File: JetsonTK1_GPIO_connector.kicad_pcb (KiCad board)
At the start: 2 copper layers, 50 x 80 mm, 79 parts, among them J1 Screw_Terminal_1x03, P1 CONN_01X25, P10 CONN_01X10, P11 CONN_01X02, P12 CONN_01X03, P2 CONN_02X25, P3 CONN_02X25, P4 CONN_01X01, P5 CONN_01X04, P6 CONN_01X04, P7 CONN_01X04, P8 CONN_01X04, P9 CONN_02X10, Q1 BSS138PS, Q2 BSS138PS, Q3 BSS138PS, U1 TXB0108PW, U2 PCAL9555APW, U3 TXB0108PW, U4 MCP25625-E/SS, Y1 Crystal_GND24

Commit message: 進捗
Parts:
- removed Q1, Q2, Q3: BSS138PS, SMD_Packages:SOT363
- removed the R10 at (158.7, 52.9)
- removed the R11 at (114.9, 99.5)
- removed the R13 at (160.2, 64.6)
- removed the R15 at (158.7, 58.7)
- removed the R17 at (136.1, 87.1)
- removed the R3 at (124.9, 93.2)
- removed the R4 at (139.4, 81.3)
- removed the R5 at (121.8, 93.2)
- removed the R6 at (118.1, 99.5)
- removed the R7 at (111.8, 99.5)
- removed the R8 at (161.8, 52.9)
- removed the R9 at (136.4, 81.3)
- added C15: C, Capacitors_SMD:C_0603, F.Cu at (68.4, 92.9)
- added C16: C, Capacitors_SMD:C_0603, F.Cu at (74.2, 91.5)
- added C6: C, Capacitors_SMD:C_0603, F.Cu at (73.8, 137.2)
- added C7: C, Capacitors_SMD:C_0603, F.Cu at (79.6, 135.8)
- added C8: C, Capacitors_SMD:C_0603, F.Cu at (73.8, 129.7)
- added C9: C, Capacitors_SMD:C_0603, F.Cu at (79.6, 128.3)
- added R14: R, Resistors_SMD:R_0603, F.Cu at (83.1, 135.1)
- added R19: R, Resistors_SMD:R_0603, F.Cu at (83.1, 127.6)
- added R25: R, Resistors_SMD:R_0603, F.Cu at (77.7, 90.8)
- added U4: PCA9306, Housings_SSOP:MSOP-8_3x3mm_Pitch0.65mm, F.Cu at (78.0, 138.5)
- added U5: PCA9306, Housings_SSOP:MSOP-8_3x3mm_Pitch0.65mm, F.Cu at (78.0, 131.0)
- added U7: PCA9306, Housings_SSOP:MSOP-8_3x3mm_Pitch0.65mm, F.Cu at (72.6, 94.2)
- JP1, JP2, JP3, JP4, JP5, JP6, JP7, JP8: moved to B.Cu
- P10: footprint Pin_Headers:Pin_Header_Straight_1x10 -> Connectors_JST:JST_XH_B10B-XH-A_10x2.50mm_Straight
- P5, P6, P7, P8: footprint Pin_Headers:Pin_Header_Straight_1x04 -> Connectors_JST:JST_XH_B04B-XH-A_04x2.50mm_Straight
- P9: footprint Pin_Headers:Pin_Header_Straight_2x10 -> Connect:IDC_Header_Straight_20pins
- moved P5 186.0 mm to (89.5, 137.0), turned to 0 degrees
- moved U3 174.0 mm to (67.0, 145.0), turned to 315 degrees
- moved P7 173.4 mm to (89.5, 114.5), turned to 0 degrees
- moved P8 173.2 mm to (89.5, 122.0), turned to 0 degrees
- moved P6 173.0 mm to (89.5, 129.5), turned to 0 degrees
- moved U1 168.0 mm to (68.8, 104.7)
- moved P1 165.8 mm to (51.5, 100.5)
- moved P2 165.8 mm to (53.5, 100.5)
- moved P3 165.8 mm to (57.5, 100.5)
- moved Y1 165.1 mm to (70.4, 112.5)
- moved P9 164.2 mm to (70.0, 77.0), turned to 0 degrees
- moved U6 163.6 mm to (82.6, 103.7)
- moved U2 162.6 mm to (80.7, 86.0), turned to 270 degrees
- moved J1 162.2 mm to (94.8, 107.8), turned to 90 degrees
- moved P10 156.0 mm to (97.0, 151.0), turned to 180 degrees
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- renumbered C6 to C10, C7 to C11, C8 to C12, C9 to C13, C10 to C14, R22 to R10, R23 to R11, R24 to R12, R25 to R13, R26 to R15, R27 to R16, R28 to R17, R29 to R18, R30 to R20, R31 to R21, R32 to R22, R33 to R23, R34 to R24, R35 to R26, R36 to R27, R12 to R3, R14 to R4, R16 to R5, R18 to R6, R19 to R7, R20 to R8, R21 to R9, U4 to U6
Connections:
- P1 pad 1: Net-(P1-Pad1) -> (no net)
- P1 pad 10: Net-(P1-Pad10) -> (no net)
- P1 pad 11: Net-(P1-Pad11) -> (no net)
- P1 pad 13: Net-(P1-Pad13) -> (no net)
- P1 pad 14: Net-(P1-Pad14) -> (no net)
- P1 pad 16: Net-(P1-Pad16) -> (no net)
- P1 pad 17: Net-(P1-Pad17) -> (no net)
- P1 pad 19: Net-(P1-Pad19) -> (no net)
- P1 pad 2: Net-(P1-Pad2) -> (no net)
- P1 pad 20: Net-(P1-Pad20) -> (no net)
- P1 pad 21: Net-(P1-Pad21) -> (no net)
- P1 pad 22: Net-(P1-Pad22) -> (no net)
- P1 pad 23: Net-(P1-Pad23) -> (no net)
- P1 pad 24: Net-(P1-Pad24) -> (no net)
- P1 pad 25: Net-(P1-Pad25) -> (no net)
- P1 pad 4: Net-(P1-Pad4) -> (no net)
- P1 pad 5: Net-(P1-Pad5) -> (no net)
- P1 pad 7: Net-(P1-Pad7) -> (no net)
- P1 pad 8: Net-(P1-Pad8) -> (no net)
- P2 pad 1: Net-(P2-Pad1) -> (no net)
- P2 pad 10: Net-(P2-Pad10) -> (no net)
- P2 pad 11: Net-(P2-Pad11) -> (no net)
- P2 pad 12: Net-(P2-Pad12) -> (no net)
- P2 pad 13: Net-(P2-Pad13) -> (no net)
- P2 pad 16: Net-(P2-Pad16) -> (no net)
- P2 pad 17: Net-(P2-Pad17) -> (no net)
- P2 pad 18: Net-(P2-Pad18) -> (no net)
- P2 pad 19: Net-(P2-Pad19) -> (no net)
- P2 pad 20: Net-(P2-Pad20) -> (no net)
- P2 pad 22: Net-(P2-Pad22) -> (no net)
- P2 pad 23: Net-(P2-Pad23) -> (no net)
- P2 pad 24: Net-(P2-Pad24) -> (no net)
- P2 pad 26: Net-(P2-Pad26) -> (no net)
- P2 pad 27: Net-(P2-Pad27) -> (no net)
- P2 pad 29: Net-(P2-Pad29) -> (no net)
- P2 pad 3: Net-(P2-Pad3) -> (no net)
- P2 pad 4: Net-(P2-Pad4) -> (no net)
- P2 pad 42: Net-(P2-Pad42) -> (no net)
- P2 pad 43: Net-(P2-Pad43) -> (no net)
- P2 pad 44: Net-(P2-Pad44) -> (no net)
- P2 pad 45: Net-(P2-Pad45) -> (no net)
- P2 pad 46: Net-(P2-Pad46) -> (no net)
- P2 pad 47: Net-(P2-Pad47) -> (no net)
- P2 pad 48: Net-(P2-Pad48) -> (no net)
- P2 pad 49: Net-(P2-Pad49) -> (no net)
- P2 pad 6: Net-(P2-Pad6) -> (no net)
- P3 pad 11: Net-(P3-Pad11) -> (no net)
- P3 pad 12: Net-(P3-Pad12) -> (no net)
- P3 pad 14: Net-(P3-Pad14) -> (no net)
- P3 pad 21: Net-(P3-Pad21) -> (no net)
- P3 pad 23: Net-(P3-Pad23) -> (no net)
- P3 pad 27: Net-(P3-Pad27) -> (no net)
- P3 pad 28: Net-(P3-Pad28) -> (no net)
- P3 pad 29: Net-(P3-Pad29) -> (no net)
- P3 pad 32: Net-(P3-Pad32) -> (no net)
- P3 pad 33: Net-(P3-Pad33) -> (no net)
- P3 pad 34: Net-(P3-Pad34) -> (no net)
- P3 pad 35: Net-(P3-Pad35) -> (no net)
- P3 pad 38: Net-(P3-Pad38) -> (no net)
- P3 pad 39: Net-(P3-Pad39) -> (no net)
- P3 pad 40: Net-(P3-Pad40) -> (no net)
- P3 pad 41: Net-(P3-Pad41) -> (no net)
- P3 pad 44: Net-(P3-Pad44) -> (no net)
- P3 pad 45: Net-(P3-Pad45) -> (no net)
- P3 pad 46: Net-(P3-Pad46) -> (no net)
- P3 pad 47: Net-(P3-Pad47) -> (no net)
- P3 pad 50: Net-(P3-Pad50) -> (no net)
- P3 pad 9: Net-(P3-Pad9) -> (no net)
- U1 pad 12: Net-(U1-Pad12) -> (no net)
- U1 pad 13: Net-(U1-Pad13) -> (no net)
- U1 pad 14: Net-(U1-Pad14) -> (no net)
- U1 pad 7: Net-(U1-Pad7) -> (no net)
- U1 pad 8: Net-(U1-Pad8) -> (no net)
- U1 pad 9: Net-(U1-Pad9) -> (no net)
- U3 pad 1: GPIO_PH1 -> GPIO_PU0
- U3 pad 3: GPIO_PU0 -> GPIO_PU1
- U3 pad 4: GPIO_PU1 -> GPIO_PU2
- U3 pad 5: GPIO_PU2 -> GPIO_PU3
- U3 pad 6: GPIO_PU3 -> GPIO_PU4
- U3 pad 7: GPIO_PU4 -> GPIO_PU5
- U3 pad 8: GPIO_PU5 -> GPIO_PU6
- U3 pad 9: GPIO_PU6 -> GPIO_PH1
- U6 pad 11: Net-(U4-Pad11) -> (no net)
- U6 pad 12: Net-(U4-Pad12) -> (no net)
- U6 pad 2: Net-(U4-Pad2) -> (no net)
- U6 pad 22: Net-(U4-Pad22) -> (no net)
- U6 pad 23: Net-(U4-Pad23) -> (no net)
- U6 pad 25: Net-(U4-Pad25) -> (no net)
- U6 pad 6: Net-(U4-Pad6) -> (no net)
- U6 pad 7: Net-(U4-Pad7) -> (no net)
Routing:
- net GND: track 9.99 -> 133.7 mm
- net +1V8: track 0.00 -> 56.3 mm
- net I2C_SDA_3V3: track 0.00 -> 39.5 mm
- net I2C_SCL_3V3: track 0.00 -> 37.9 mm
- net I2C_SDA_1V8: track 0.00 -> 36.6 mm
- net I2C_SCL_1V8: track 0.00 -> 33.6 mm
- net PWR_I2C_SDA: track 0.00 -> 27.3 mm, vias 0 -> 2
- net GEN1_I2C_SDA: track 0.00 -> 26.7 mm, vias 0 -> 2
- net GEN1_I2C_SCL: track 0.00 -> 24.2 mm, vias 0 -> 1
- net PWR_I2C_SCL: track 0.00 -> 23.7 mm, vias 0 -> 1
- net Net-(P9-Pad3): track 0.00 -> 21.6 mm, vias 0 -> 1
- net GPIO_PU0: track 0.00 -> 19.5 mm
- net Net-(P9-Pad17): track 0.00 -> 19.0 mm, vias 0 -> 1
- net Net-(P9-Pad5): track 0.00 -> 18.5 mm, vias 0 -> 1
- net /logic_conv_1/HV2: track 0.00 -> 18.4 mm, vias 0 -> 2
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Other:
- board size 50 x 80 mm -> 50 x 85 mm

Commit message: 進捗
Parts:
- J1: value Screw_Terminal_1x03 -> Screw_Terminal_1x02; footprint Terminal_Blocks:TerminalBlock_Pheonix_MKDS1.5-3pol -> Terminal_Blocks:TerminalBlock_Pheonix_MKDS1.5-2pol
- Y1: value Crystal_GND24 -> Crystal_Small; footprint Crystals:Crystal_SMD_5032_4Pads -> Crystals:Crystal_HC49-U_Vertical
- moved P11 26.3 mm to (94.0, 95.0), turned to 270 degrees
- moved R22 25.7 mm to (97.0, 95.0), turned to 270 degrees
- moved C14 24.0 mm to (82.8, 95.5), turned to 0 degrees
- moved JP8 21.2 mm to (85.7, 143.9)
- moved C13 17.7 mm to (79.8, 95.5), turned to 180 degrees
- moved Y1 17.5 mm to (81.3, 98.8)
- moved C12 12.0 mm to (85.3, 112.0), turned to 0 degrees
- moved R2 11.0 mm to (79.0, 112.0), turned to 0 degrees
- moved C11 10.6 mm to (88.4, 103.4), turned to 270 degrees
- moved C10 10.5 mm to (82.0, 112.0)
- moved JP3 9.89 mm to (85.7, 128.9)
- moved JP2 9.31 mm to (85.7, 136.4)
- moved C4 5.60 mm to (91.4, 88.2)
- moved U2 5.60 mm to (86.3, 86.0)
- moved JP6 4.11 mm to (70.0, 85.9)
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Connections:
- P11 pad 2: Net-(J1-Pad2) -> Net-(J1-Pad1)
- P12 pad 1: Net-(J1-Pad1) -> Net-(J1-Pad2)
- P12 pad 2: Net-(J1-Pad2) -> Net-(J1-Pad1)
- R22 pad 2: Net-(J1-Pad1) -> Net-(J1-Pad2)
- U6 pad 3: Net-(J1-Pad2) -> Net-(J1-Pad1)
- U6 pad 4: Net-(J1-Pad1) -> Net-(J1-Pad2)
- Y1 pad 1: Net-(C14-Pad2) -> Net-(C13-Pad2)
- Y1 pad 2: GND -> Net-(C14-Pad2)
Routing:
- net GND: track 133.7 -> 231.7 mm, vias 0 -> 6
- net +3V3: track 12.5 -> 72.0 mm
- net +1V8: track 56.3 -> 96.5 mm, vias 0 -> 2
- net +5V: track 4.89 -> 42.5 mm
- net CAM_I2C_SDA: track 0.00 -> 31.7 mm, vias 0 -> 3
- net Net-(C5-Pad1): track 3.09 -> 34.5 mm, vias 0 -> 1
- net CAM_I2C_SCL: track 0.00 -> 30.0 mm
- net Net-(J1-Pad1): track 0.00 -> 24.1 mm
- net /logic_conv_3/VH: track 11.0 -> 33.7 mm, vias 0 -> 1
- net /SPI-CAN/VDD: track 0.00 -> 19.2 mm
- net Net-(J1-Pad2): track 0.00 -> 17.6 mm
- net /SPI-CAN/~CS: track 0.00 -> 13.9 mm, vias 0 -> 2
- net /SPI-CAN/SO: track 0.00 -> 11.7 mm, vias 0 -> 2
- net /SPI-CAN/SI: track 0.00 -> 10.4 mm, vias 0 -> 2
- net /SPI-CAN/~INT: track 0.00 -> 8.64 mm
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- added copper zone on B.Cu, net GND
- added copper zone on F.Cu, net GND
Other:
- board text added: "3.3V"
- board text added: "5V"
- board text added: "A0"
- board text added: "A1"
- board text added: "A2"
- board text added: "GND"
- board text added: "GPIO"
- board text added: "I2C"
- board text added: "I2C_1.8V"
- board text added: "I2C_3.3V"
- board text added: "PH1"
- board text added: "PU0"
- board text added: "PU1"
- board text added: "PU2"
- board text added: "PU3"
- board text added: "PU4"
- board text added: "PU5"
- board text added: "PU6"
- board text added: "SCL"
- board text added: "SDA"
- board text added: "VDD"

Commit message: LED以外接続完了
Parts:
- moved P12 20.5 mm to (87.9, 101.4), turned to 180 degrees
- moved R1 2.20 mm to (65.1, 111.0)
- moved C10 2.20 mm to (80.9, 113.9)
- moved C12 2.20 mm to (84.2, 113.9)
- moved C13 2.20 mm to (78.7, 97.4)
- moved C14 2.20 mm to (81.7, 97.4)
- moved R2 2.20 mm to (77.9, 113.9)
- moved U1 2.20 mm to (67.8, 106.6)
- moved U6 2.20 mm to (80.9, 108.2)
- moved Y1 2.20 mm to (80.2, 100.7)
- moved C1 2.20 mm to (65.2, 102.1)
- moved C2 2.20 mm to (70.2, 102.1)
- moved C11 1.92 mm to (87.2, 104.9)
- moved JP1 1.00 mm to (75.6, 115.3), turned to 0 degrees
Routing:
- net GND: track 231.7 -> 392.7 mm, vias 6 -> 12
- net +5V: track 42.5 -> 98.0 mm, vias 0 -> 2
- net +1V8: track 96.5 -> 127.0 mm, vias 2 -> 3
- net +3V3: track 72.0 -> 100.7 mm, vias 0 -> 2
- net /SPI-CAN/VDD: track 19.2 -> 39.4 mm, vias 0 -> 2
- net /logic_conv_3/VH: track 33.7 -> 50.3 mm, vias 1 -> 2
- net GPIO_PK2: track 4.24 -> 12.4 mm
- net TS_SPI_CS_L: track 3.64 -> 10.3 mm, vias 0 -> 1
- net Net-(J1-Pad1): track 24.1 -> 30.2 mm
- net TS_SPI_MISO: track 7.29 -> 5.40 mm
- net Net-(J1-Pad2): track 17.6 -> 19.5 mm
- net TS_SPI_SCK: track 9.44 -> 8.31 mm
- net TS_SPI_MOSI: track 6.73 -> 5.76 mm
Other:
- outline, holes or cut-outs redrawn
- board text added: "SPI"

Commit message: ver1.0完成，これでElecrow発注
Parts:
- P9: footprint Connect:IDC_Header_Straight_20pins -> Connectors_Multicomp:Multicomp_MC9A12-2034_2x10x2.54mm_Straight
- moved P4 105.3 mm to (201.7, 77.5)
- moved P12 105.1 mm to (192.9, 96.0), turned to 0 degrees
- moved JP4 105.1 mm to (195.8, 78.6)
- moved JP5 105.1 mm to (195.8, 81.4)
- moved JP7 105.1 mm to (195.8, 84.2)
- moved R12 105.1 mm to (175.8, 133.3)
- moved R15 105.1 mm to (187.8, 133.6)
- moved R17 105.1 mm to (175.8, 125.8)
- moved R20 105.1 mm to (187.8, 126.1)
- moved R23 105.1 mm to (169.8, 83.8)
- moved R26 105.1 mm to (181.8, 84.1)
- moved R7 105.1 mm to (187.8, 118.6)
- moved U2 105.1 mm to (191.3, 81.0)
- moved C15 105.1 mm to (173.4, 83.9)
- moved C3 105.1 mm to (174.4, 136.2)
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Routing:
- net GND: track 392.7 -> 446.3 mm, vias 12 -> 5
- net +3V3: track 100.7 -> 108.0 mm
- net +1V8: track 127.0 -> 133.1 mm
- net Net-(J1-Pad2): track 19.5 -> 24.1 mm
- net +5V: track 98.0 -> 93.6 mm
- net /SPI-CAN/~CS: track 13.9 -> 9.81 mm
- net /SPI-CAN/SO: track 11.7 -> 7.92 mm
- net +12V: track 0.00 -> 2.91 mm
- net /SPI-CAN/SI: track 10.4 -> 7.67 mm
- net GPIO_PK2: track 12.4 -> 10.5 mm
- net TS_SPI_MISO: track 5.40 -> 3.58 mm
- net Net-(D2-Pad1): track 0.00 -> 1.70 mm
- net Net-(D4-Pad1): track 0.00 -> 1.70 mm
- net Net-(D3-Pad1): track 0.00 -> 1.70 mm
- net /SPI-CAN/SCK: track 6.14 -> 4.51 mm
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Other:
- board text added: "1.8V"
- board text added: "12V"
- board text added: "G"
- board text added: "H"
- board text added: "L"

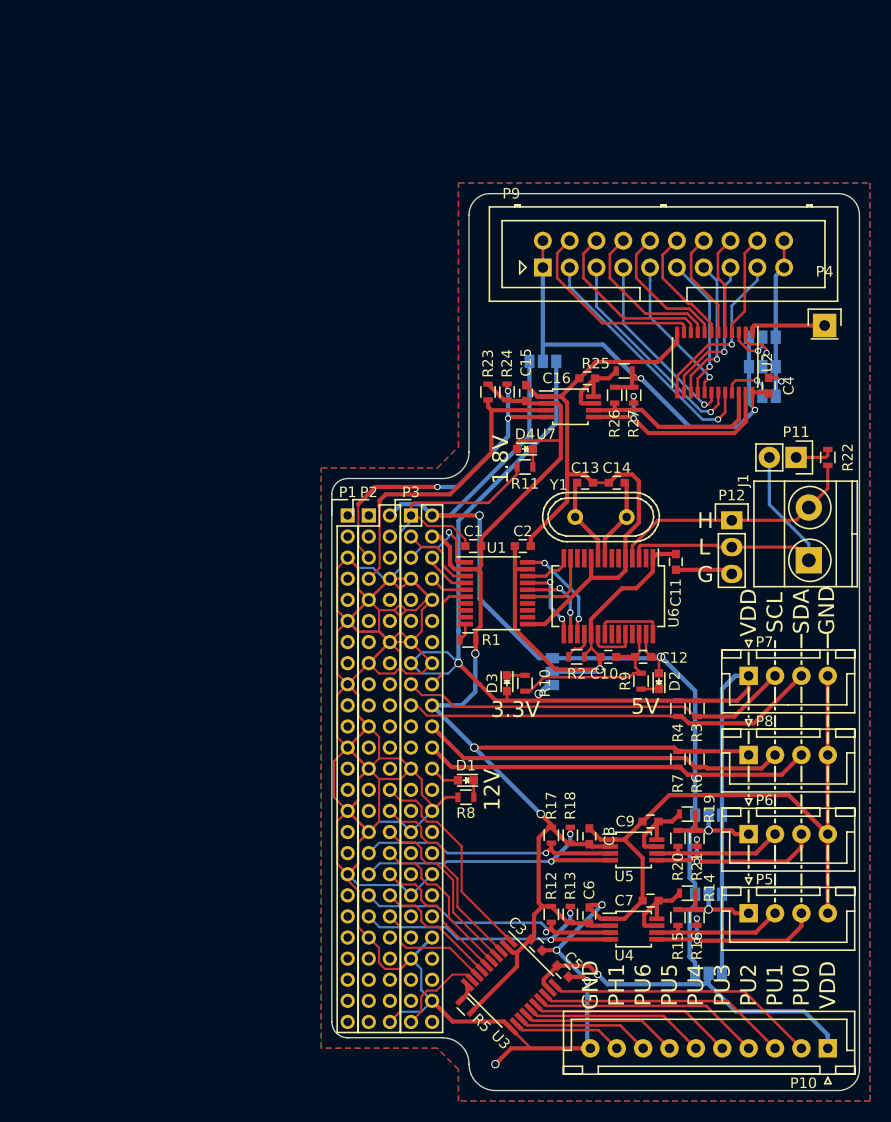
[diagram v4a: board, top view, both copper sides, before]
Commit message: via追加
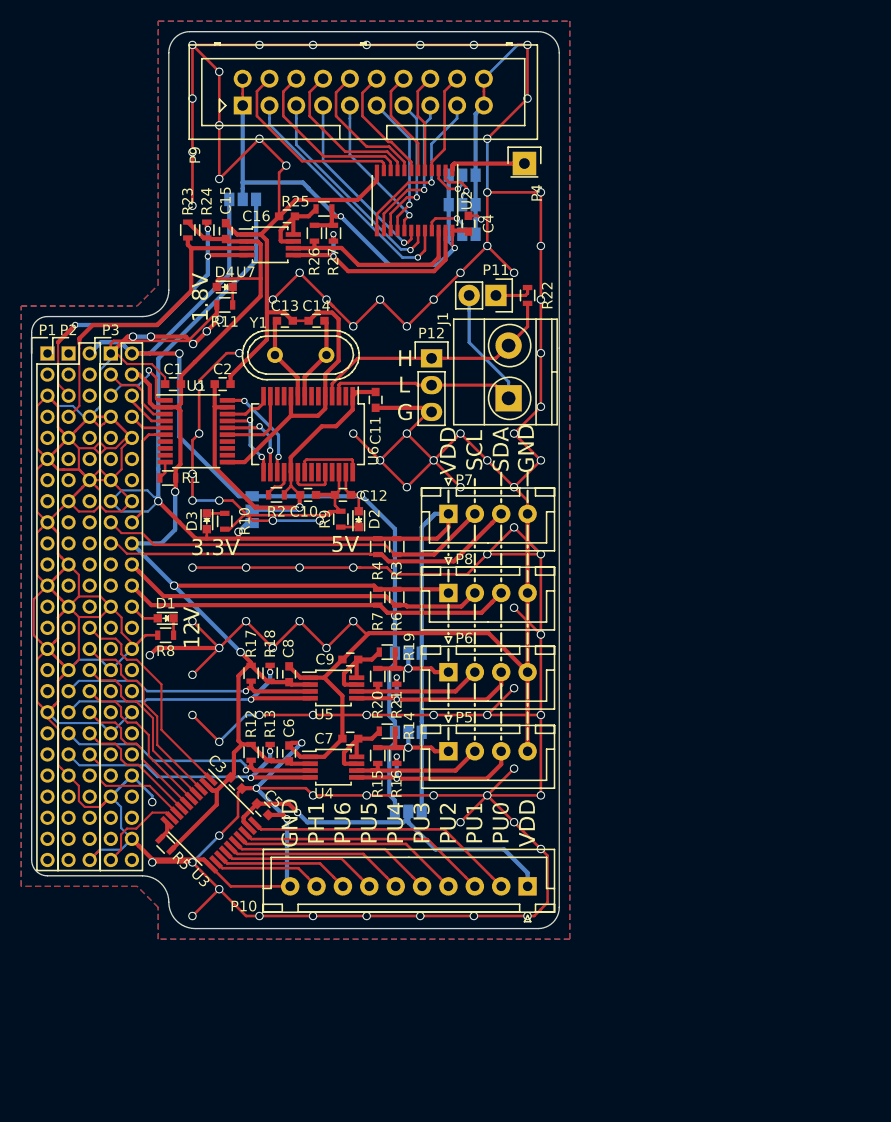
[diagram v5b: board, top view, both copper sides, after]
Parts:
- moved C1 32.3 mm to (139.9, 83.0)
- moved C15 32.3 mm to (144.9, 68.5)
- moved C4 32.3 mm to (167.9, 67.8)
- moved C6 32.3 mm to (150.9, 118.0)
- moved C8 32.3 mm to (150.9, 110.5)
- moved D4 32.3 mm to (144.8, 73.8)
- moved JP5 32.3 mm to (167.3, 66.0)
- moved JP7 32.3 mm to (167.3, 68.8)
- moved R10 32.3 mm to (144.8, 96.0)
- moved R11 32.3 mm to (144.8, 75.5)
- moved R12 32.3 mm to (147.3, 118.0)
- moved R9 32.3 mm to (155.8, 95.8)
- moved C3 32.3 mm to (145.9, 120.8)
- moved C5 32.3 mm to (148.4, 123.3)
- moved JP1 32.3 mm to (147.4, 95.0)
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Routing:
- net GND: track 446.3 -> 939.4 mm, vias 5 -> 109
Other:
- board text added: "JetsonTK1_Expand_Board @C91 Manju-Hompo Designed by @yuqlid"
- board text added: "i2c-0"
- board text added: "i2c-1"
- board text added: "i2c-4"
